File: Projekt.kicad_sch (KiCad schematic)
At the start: 98 parts, among them J1 Solar, J2 Battery, J3 USB_B_Mini, J4 INTERFACE PORT, J5 FAN, J6 JTAG, Q1 CSD19505KCS, Q1b1 CSD19505KCS, Q2 CSD19505KCS, Q2b1 CSD19505KCS, Q3 CSD19505KCS, Q3b1 CSD19505KCS, Q4 Si2306, Q5 MMBT3904 1A, Q6 MMBT3904 1A, Q7 Si2306, U1 ACS712, U10 ADS1015, U2 B1212S, U3 AMS1117-5.0, U4 AMS1117-3.3, U5 XL7005A, U6 XL7005A, U7 IR2104, U8 ESP32, U9 CH340G

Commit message: Eigentlich okay...
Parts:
- added J?: PRG, Connector_PinHeader_2.54mm:PinHeader_1x02_P2.54mm_Vertical, symbol Connector:Conn_01x02_Male
- renumbered Q1b1 to Q11, Q2b1 to Q12, Q3b1 to Q13
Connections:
- net GND: now also J?.1 (Pin_1)
- net GPIO0: now also J?.2 (Pin_2)
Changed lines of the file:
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@@
   (junction (at 44.45 154.94) (diameter 0) (color 0 0 0 0)
   )
+  (junction (at 185.42 91.44) (diameter 0) (color 0 0 0 0)
+  )
   (junction (at 86.36 24.13) (diameter 0) (color 0 0 0 0)
   )
@@
     (stroke (width 0) (type default) (color 0 0 0 0))
   )
+  (wire (pts (xy 182.88 91.44) (xy 185.42 91.44))
+    (stroke (width 0) (type default) (color 0 0 0 0))
+  )
   (wire (pts (xy 119.38 135.89) (xy 119.38 139.7))
     (stroke (width 0) (type default) (color 0 0 0 0))
@@
     (stroke (width 0) (type default) (color 0 0 0 0))
   )
+  (wire (pts (xy 187.325 88.9) (xy 187.325 92.71))
+    (stroke (width 0) (type default) (color 0 0 0 0))
+  )
   (wire (pts (xy 25.4 115.57) (xy 20.32 115.57))
     (stroke (width 0) (type default) (color 0 0 0 0))
@@
     (stroke (width 0) (type default) (color 0 0 0 0))
   )
+  (wire (pts (xy 182.88 88.9) (xy 187.325 88.9))
+    (stroke (width 0) (type default) (color 0 0 0 0))
+  )
   (wire (pts (xy 125.73 72.39) (xy 154.94 72.39))
     (stroke (width 0) (type default) (color 0 0 0 0))
@@
     (stroke (width 0) (type default) (color 0 0 0 0))
   )
+  (wire (pts (xy 185.42 91.44) (xy 185.42 93.98))
+    (stroke (width 0) (type default) (color 0 0 0 0))
+  )
   (wire (pts (xy 162.56 97.79) (xy 163.83 97.79))
     (stroke (width 0) (type default) (color 0 0 0 0))
@@
     (stroke (width 0) (type default) (color 0 0 0 0))
   )
-  (wire (pts (xy 191.77 91.44) (xy 193.04 91.44))
+  (wire (pts (xy 185.42 91.44) (xy 193.04 91.44))
     (stroke (width 0) (type default) (color 0 0 0 0))
   )
@@
     )
   )
-  (global_label "GPIO0" (shape input) (at 191.77 91.44 180) (fields_autoplaced)
+  (global_label "GPIO0" (shape input) (at 185.42 93.98 180) (fields_autoplaced)
     (effects (font (size 1.27 1.27)) (justify right))
-    (property "Intersheet References" "${INTERSHEET_REFS}" (id 0) (at 183.6721 91.3606 0)
+    (property "Intersheet References" "${INTERSHEET_REFS}" (id 0) (at 177.3221 93.9006 0)
       (effects (font (size 1.27 1.27)) (justify right) hide)
     )
@@
   (symbol (lib_id "footprint:CSD19505KCS") (at 83.82 113.03 270) (unit 1)
     (in_bom yes) (on_board yes)
-    (property "Reference" "Q1b1" (id 0) (at 80.645 111.125 90))
+    (property "Reference" "Q11" (id 0) (at 80.645 111.125 90))
     (property "Value" "CSD19505KCS" (id 1) (at 83.82 119.38 90))
     (property "Footprint" "Package_TO_SOT_THT:TO-220-3_Vertical" (id 2) (at 68.834 121.412 90)
@@
   (symbol (lib_id "footprint:CSD19505KCS") (at 104.14 127 0) (unit 1)
     (in_bom yes) (on_board yes)
-    (property "Reference" "Q2b1" (id 0) (at 102.235 129.54 90))
+    (property "Reference" "Q12" (id 0) (at 102.235 129.54 90))
     (property "Value" "CSD19505KCS" (id 1) (at 110.49 127 90))
     (property "Footprint" "Package_TO_SOT_THT:TO-220-3_Vertical" (id 2) (at 112.522 141.986 90)
@@
   (symbol (lib_id "footprint:CSD19505KCS") (at 104.14 143.51 0) (unit 1)
     (in_bom yes) (on_board yes)
-    (property "Reference" "Q3" (id 0) (at 102.235 140.335 90))
+    (property "Reference" "Q3" (id 0) (at 102.235 146.05 90))
     (property "Value" "CSD19505KCS" (id 1) (at 110.49 143.51 90))
     (property "Footprint" "Package_TO_SOT_THT:TO-220-3_Vertical" (id 2) (at 112.522 158.496 90)
@@
     (pin "2")
   )
+  (symbol (lib_id "power:GND") (at 187.325 92.71 0) (unit 1)
+    (in_bom yes) (on_board yes) (fields_autoplaced)
+    (property "Reference" "#PWR?" (id 0) (at 187.325 99.06 0)
+      (effects (font (size 1.27 1.27)) hide)
+    )
+    (property "Value" "GND" (id 1) (at 187.325 97.79 0))
+    (property "Footprint" "" (id 2) (at 187.325 92.71 0)
+      (effects (font (size 1.27 1.27)) hide)
+    )
+    (property "Datasheet" "" (id 3) (at 187.325 92.71 0)
+      (effects (font (size 1.27 1.27)) hide)
+    )
+    (pin "1")
+  )
   (symbol (lib_id "Device:R_Small") (at 166.37 97.79 90) (unit 1)
     (in_bom yes) (on_board yes)
@@
     (pin "1")
   )
+  (symbol (lib_id "Connector:Conn_01x02_Male") (at 177.8 88.9 0) (unit 1)
+    (in_bom yes) (on_board yes)
+    (property "Reference" "J?" (id 0) (at 177.8 93.98 0)
+      (effects (font (size 1.27 1.27)) (justify right))
+    )
+    (property "Value" "PRG" (id 1) (at 179.07 86.36 0)
+      (effects (font (size 1.27 1.27)) (justify right))
+    )
+    (property "Footprint" "Connector_PinHeader_2.54mm:PinHeader_1x02_P2.54mm_Vertical" (id 2) (at 177.8 88.9 0)
+      (effects (font (size 1.27 1.27)) hide)
+    )
+    (property "Datasheet" "~" (id 3) (at 177.8 88.9 0)
+      (effects (font (size 1.27 1.27)) hide)
+    )
+    (pin "1")
+    (pin "2")
+  )
   (symbol (lib_id "Device:C_Small") (at 129.54 149.86 0) (unit 1)
     (in_bom yes) (on_board yes)
@@
   (symbol (lib_id "footprint:CSD19505KCS") (at 104.14 143.51 0) (unit 1)
     (in_bom yes) (on_board yes)
-    (property "Reference" "Q3b1" (id 0) (at 102.235 140.335 90))
+    (property "Reference" "Q13" (id 0) (at 102.235 140.335 90))
     (property "Value" "CSD19505KCS" (id 1) (at 110.49 143.51 90))
     (property "Footprint" "Package_TO_SOT_THT:TO-220-3_Vertical" (id 2) (at 112.522 158.496 90)
@@
       (reference "#PWR0125") (unit 1) (value "GND") (footprint "")
     )
+    (path "/c5a5ef8d-c592-47eb-bd21-ceec507b7d31"
+      (reference "#PWR?") (unit 1) (value "GND") (footprint "")
+    )
     (path "/6c036c9e-e0d1-4bac-b51b-db7b92cdf233"
       (reference "C1") (unit 1) (value "100nF") (footprint "Capacitor_SMD:C_0603_1608Metric")
@@
       (reference "J6") (unit 1) (value "JTAG") (footprint "Connector_PinHeader_1.27mm:PinHeader_2x05_P1.27mm_Vertical_SMD")
     )
+    (path "/d0f189fe-2700-4f77-8370-882eccb1f8d9"
+      (reference "J?") (unit 1) (value "PRG") (footprint "Connector_PinHeader_2.54mm:PinHeader_1x02_P2.54mm_Vertical")
+    )
     (path "/a34be4f0-cd07-4bab-9f46-bdfef665e51a"
       (reference "L1") (unit 1) (value "60uH") (footprint "Inductor_THT:L_Toroid_Vertical_L21.6mm_W11.4mm_P7.62mm_Pulse_KM-3")
@@
       (reference "Q1") (unit 1) (value "CSD19505KCS") (footprint "Package_TO_SOT_THT:TO-220-3_Vertical")
     )
-    (path "/068a26f9-efe8-4653-9ca9-597ae39bb735"
-      (reference "Q1b1") (unit 1) (value "CSD19505KCS") (footprint "Package_TO_SOT_THT:TO-220-3_Vertical")
-    )
     (path "/539c37cf-e417-4bd0-89c6-457ec992b15f"
       (reference "Q2") (unit 1) (value "CSD19505KCS") (footprint "Package_TO_SOT_THT:TO-220-3_Vertical")
     )
-    (path "/54409513-d3fa-492e-a001-a088fdce9fa5"
-      (reference "Q2b1") (unit 1) (value "CSD19505KCS") (footprint "Package_TO_SOT_THT:TO-220-3_Vertical")
-    )
     (path "/bb113282-5d8f-4b0b-a4b8-2446b034aad5"
       (reference "Q3") (unit 1) (value "CSD19505KCS") (footprint "Package_TO_SOT_THT:TO-220-3_Vertical")
     )
-    (path "/dd65f54c-87a0-4385-98b4-810c8b6410c7"
-      (reference "Q3b1") (unit 1) (value "CSD19505KCS") (footprint "Package_TO_SOT_THT:TO-220-3_Vertical")
-    )
     (path "/d518002e-8259-4f21-880a-acde968c86e4"
       (reference "Q4") (unit 1) (value "Si2306") (footprint "Package_TO_SOT_SMD:SOT-23")
@@
       (reference "Q7") (unit 1) (value "Si2306") (footprint "Package_TO_SOT_SMD:SOT-23")
     )
+    (path "/068a26f9-efe8-4653-9ca9-597ae39bb735"
+      (reference "Q11") (unit 1) (value "CSD19505KCS") (footprint "Package_TO_SOT_THT:TO-220-3_Vertical")
+    )
+    (path "/54409513-d3fa-492e-a001-a088fdce9fa5"
+      (reference "Q12") (unit 1) (value "CSD19505KCS") (footprint "Package_TO_SOT_THT:TO-220-3_Vertical")
+    )
+    (path "/dd65f54c-87a0-4385-98b4-810c8b6410c7"
+      (reference "Q13") (unit 1) (value "CSD19505KCS") (footprint "Package_TO_SOT_THT:TO-220-3_Vertical")
+    )
     (path "/c953cab7-4946-4acc-9567-3e799c6ea44c"

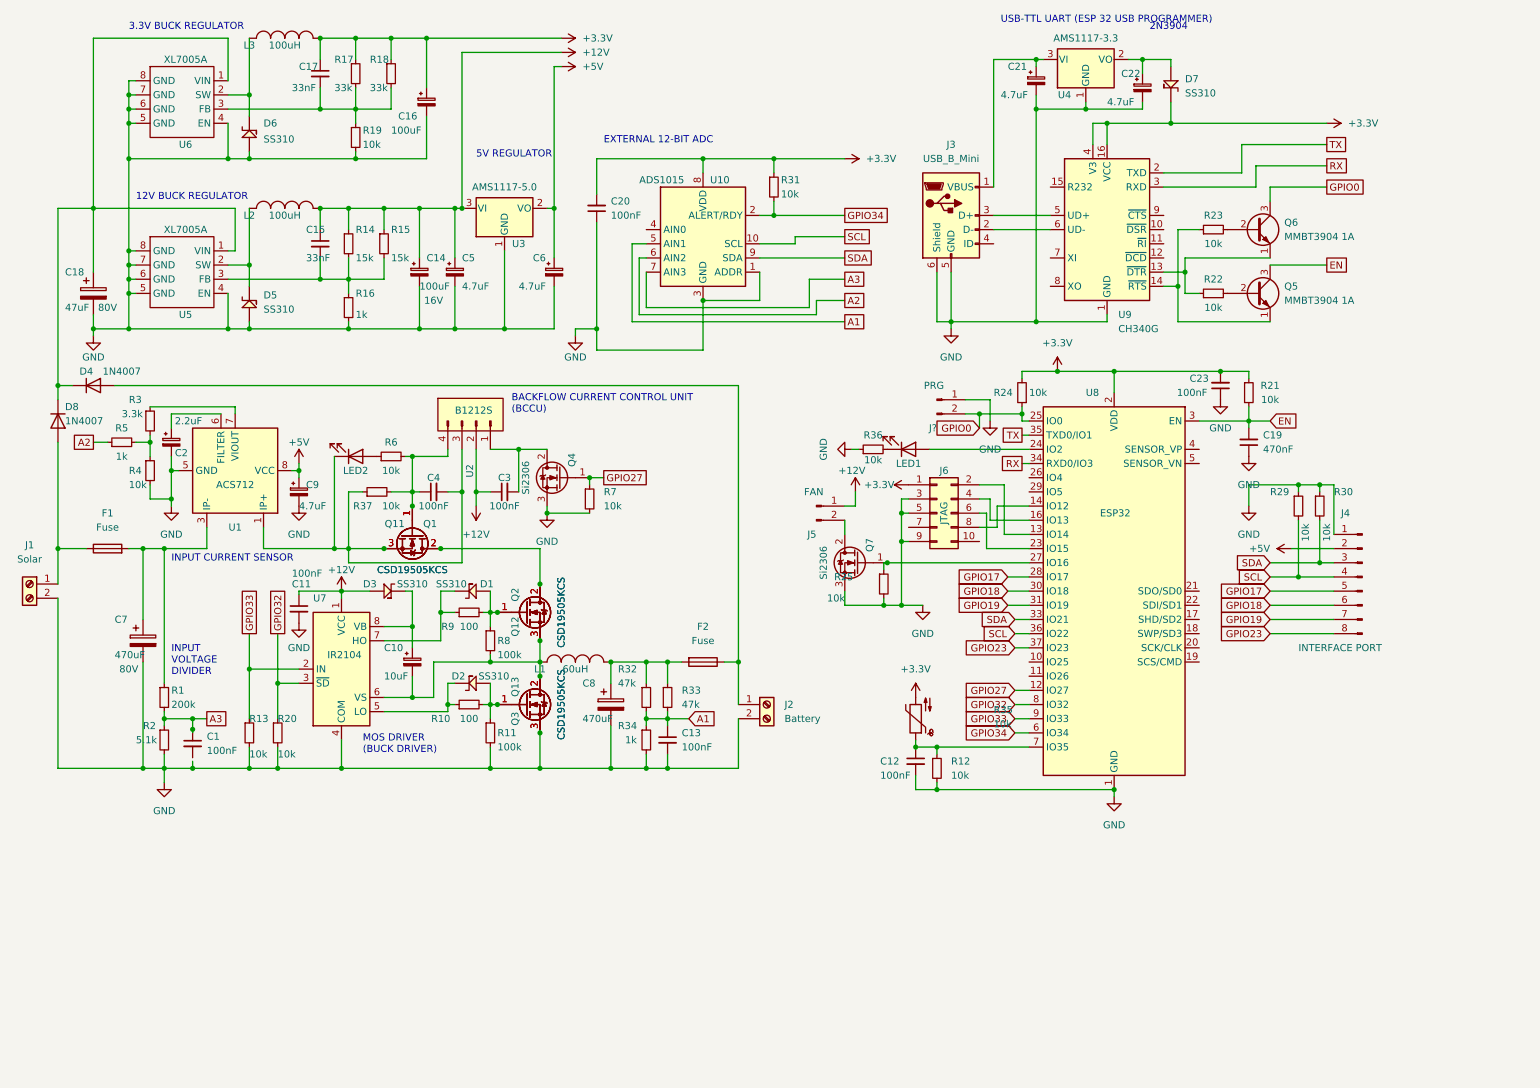
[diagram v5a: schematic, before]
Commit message: Fehlerhafte Pads entfernt und in Footprint eingebaut
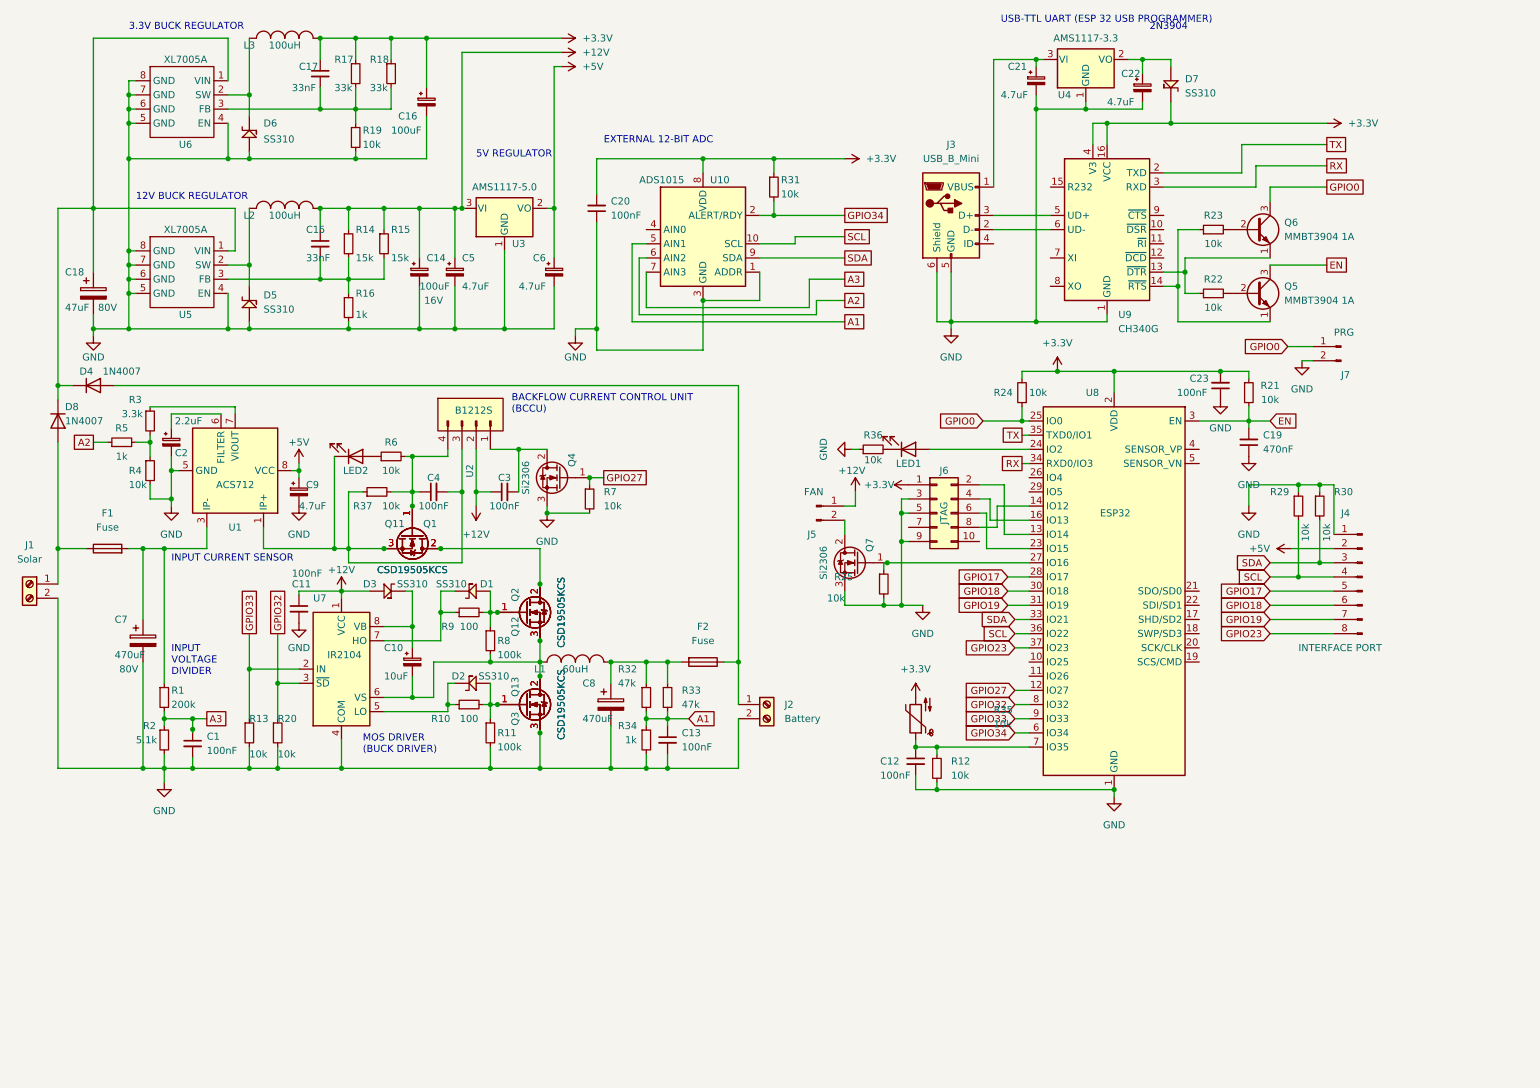
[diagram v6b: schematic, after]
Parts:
- gave numbers to parts that had none: 1
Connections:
- net GND: now also C1.2, J7.2 (Pin_2); no longer J7.1 (Pin_1)
- net GPIO0: now also J7.1 (Pin_1); no longer J7.2 (Pin_2)
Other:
- moved on the sheet: J7
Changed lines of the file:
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@@
   (junction (at 44.45 154.94) (diameter 0) (color 0 0 0 0)
   )
-  (junction (at 185.42 91.44) (diameter 0) (color 0 0 0 0)
-  )
   (junction (at 86.36 24.13) (diameter 0) (color 0 0 0 0)
   )
@@
   (junction (at 67.31 24.13) (diameter 0) (color 0 0 0 0)
   )
-  (junction (at 193.04 91.44) (diameter 0) (color 0 0 0 0)
-  )
   (junction (at 72.39 115.57) (diameter 0) (color 0 0 0 0)
   )
@@
   (junction (at 125.73 154.94) (diameter 0) (color 0 0 0 0)
   )
+  (junction (at 193.04 92.71) (diameter 0) (color 0 0 0 0)
+  )
   (junction (at 106.68 138.43) (diameter 0) (color 0 0 0 0)
   )
@@
     (stroke (width 0) (type default) (color 0 0 0 0))
   )
+  (wire (pts (xy 240.665 79.375) (xy 245.11 79.375))
+    (stroke (width 0) (type default) (color 0 0 0 0))
+  )
   (wire (pts (xy 26.67 54.61) (xy 20.32 54.61))
     (stroke (width 0) (type default) (color 0 0 0 0))
@@
     (stroke (width 0) (type default) (color 0 0 0 0))
   )
-  (wire (pts (xy 182.88 91.44) (xy 185.42 91.44))
-    (stroke (width 0) (type default) (color 0 0 0 0))
-  )
   (wire (pts (xy 119.38 135.89) (xy 119.38 139.7))
     (stroke (width 0) (type default) (color 0 0 0 0))
@@
     (stroke (width 0) (type default) (color 0 0 0 0))
   )
-  (wire (pts (xy 193.04 90.17) (xy 193.04 91.44))
-    (stroke (width 0) (type default) (color 0 0 0 0))
-  )
-  (wire (pts (xy 193.04 91.44) (xy 193.04 92.71))
+  (wire (pts (xy 193.04 90.17) (xy 193.04 92.71))
     (stroke (width 0) (type default) (color 0 0 0 0))
   )
@@
     (stroke (width 0) (type default) (color 0 0 0 0))
   )
+  (wire (pts (xy 243.205 81.915) (xy 245.11 81.915))
+    (stroke (width 0) (type default) (color 0 0 0 0))
+  )
   (wire (pts (xy 33.02 34.29) (xy 33.02 36.83))
     (stroke (width 0) (type default) (color 0 0 0 0))
@@
     (stroke (width 0) (type default) (color 0 0 0 0))
   )
+  (wire (pts (xy 186.055 92.71) (xy 193.04 92.71))
+    (stroke (width 0) (type default) (color 0 0 0 0))
+  )
   (wire (pts (xy 39.37 154.94) (xy 39.37 157.48))
     (stroke (width 0) (type default) (color 0 0 0 0))
@@
     (stroke (width 0) (type default) (color 0 0 0 0))
   )
-  (wire (pts (xy 187.325 88.9) (xy 187.325 92.71))
-    (stroke (width 0) (type default) (color 0 0 0 0))
-  )
   (wire (pts (xy 25.4 115.57) (xy 20.32 115.57))
     (stroke (width 0) (type default) (color 0 0 0 0))
@@
     (stroke (width 0) (type default) (color 0 0 0 0))
   )
-  (wire (pts (xy 182.88 88.9) (xy 187.325 88.9))
-    (stroke (width 0) (type default) (color 0 0 0 0))
-  )
   (wire (pts (xy 125.73 72.39) (xy 154.94 72.39))
     (stroke (width 0) (type default) (color 0 0 0 0))
@@
     (stroke (width 0) (type default) (color 0 0 0 0))
   )
-  (wire (pts (xy 44.45 154.94) (xy 44.45 153.67))
+  (wire (pts (xy 44.45 153.035) (xy 44.45 154.94))
     (stroke (width 0) (type default) (color 0 0 0 0))
   )
@@
     (stroke (width 0) (type default) (color 0 0 0 0))
   )
-  (wire (pts (xy 185.42 91.44) (xy 185.42 93.98))
-    (stroke (width 0) (type default) (color 0 0 0 0))
-  )
   (wire (pts (xy 162.56 97.79) (xy 163.83 97.79))
     (stroke (width 0) (type default) (color 0 0 0 0))
@@
     (stroke (width 0) (type default) (color 0 0 0 0))
   )
-  (wire (pts (xy 185.42 91.44) (xy 193.04 91.44))
-    (stroke (width 0) (type default) (color 0 0 0 0))
-  )
   (wire (pts (xy 115.57 102.87) (xy 115.57 104.14))
     (stroke (width 0) (type default) (color 0 0 0 0))
@@
     )
   )
+  (global_label "GPIO0" (shape input) (at 240.665 79.375 180) (fields_autoplaced)
+    (effects (font (size 1.27 1.27)) (justify right))
+    (property "Intersheet References" "${INTERSHEET_REFS}" (id 0) (at 232.5671 79.4544 0)
+      (effects (font (size 1.27 1.27)) (justify right) hide)
+    )
+  )
   (global_label "A2" (shape passive) (at 161.29 71.12 0) (fields_autoplaced)
     (effects (font (size 1.27 1.27)) (justify left))
@@
     )
   )
-  (global_label "GPIO0" (shape input) (at 185.42 93.98 180) (fields_autoplaced)
+  (global_label "GPIO0" (shape input) (at 186.055 92.71 180) (fields_autoplaced)
     (effects (font (size 1.27 1.27)) (justify right))
-    (property "Intersheet References" "${INTERSHEET_REFS}" (id 0) (at 177.3221 93.9006 0)
+    (property "Intersheet References" "${INTERSHEET_REFS}" (id 0) (at 177.9571 92.7894 0)
       (effects (font (size 1.27 1.27)) (justify right) hide)
     )
@@
     (pin "2")
   )
-  (symbol (lib_id "power:GND") (at 187.325 92.71 0) (unit 1)
+  (symbol (lib_id "power:GND") (at 243.205 81.915 0) (unit 1)
     (in_bom yes) (on_board yes) (fields_autoplaced)
-    (property "Reference" "#PWR?" (id 0) (at 187.325 99.06 0)
+    (property "Reference" "#PWR0126" (id 0) (at 243.205 88.265 0)
       (effects (font (size 1.27 1.27)) hide)
     )
-    (property "Value" "GND" (id 1) (at 187.325 97.79 0))
-    (property "Footprint" "" (id 2) (at 187.325 92.71 0)
+    (property "Value" "GND" (id 1) (at 243.205 86.995 0))
+    (property "Footprint" "" (id 2) (at 243.205 81.915 0)
       (effects (font (size 1.27 1.27)) hide)
     )
-    (property "Datasheet" "" (id 3) (at 187.325 92.71 0)
+    (property "Datasheet" "" (id 3) (at 243.205 81.915 0)
       (effects (font (size 1.27 1.27)) hide)
     )
@@
     (pin "1")
   )
-  (symbol (lib_id "Connector:Conn_01x02_Male") (at 177.8 88.9 0) (unit 1)
+  (symbol (lib_id "Connector:Conn_01x02_Male") (at 250.19 79.375 0) (mirror y) (unit 1)
     (in_bom yes) (on_board yes)
-    (property "Reference" "J?" (id 0) (at 177.8 93.98 0)
+    (property "Reference" "J7" (id 0) (at 250.19 84.455 0)
       (effects (font (size 1.27 1.27)) (justify right))
     )
-    (property "Value" "PRG" (id 1) (at 179.07 86.36 0)
+    (property "Value" "PRG" (id 1) (at 248.92 76.835 0)
       (effects (font (size 1.27 1.27)) (justify right))
     )
-    (property "Footprint" "Connector_PinHeader_2.54mm:PinHeader_1x02_P2.54mm_Vertical" (id 2) (at 177.8 88.9 0)
+    (property "Footprint" "Connector_PinHeader_2.54mm:PinHeader_1x02_P2.54mm_Vertical" (id 2) (at 250.19 79.375 0)
       (effects (font (size 1.27 1.27)) hide)
     )
-    (property "Datasheet" "~" (id 3) (at 177.8 88.9 0)
+    (property "Datasheet" "~" (id 3) (at 250.19 79.375 0)
       (effects (font (size 1.27 1.27)) hide)
     )
@@
     )
     (path "/c5a5ef8d-c592-47eb-bd21-ceec507b7d31"
-      (reference "#PWR?") (unit 1) (value "GND") (footprint "")
+      (reference "#PWR0126") (unit 1) (value "GND") (footprint "")
     )
     (path "/6c036c9e-e0d1-4bac-b51b-db7b92cdf233"
@@
     )
     (path "/d0f189fe-2700-4f77-8370-882eccb1f8d9"
-      (reference "J?") (unit 1) (value "PRG") (footprint "Connector_PinHeader_2.54mm:PinHeader_1x02_P2.54mm_Vertical")
+      (reference "J7") (unit 1) (value "PRG") (footprint "Connector_PinHeader_2.54mm:PinHeader_1x02_P2.54mm_Vertical")
     )
     (path "/a34be4f0-cd07-4bab-9f46-bdfef665e51a"
